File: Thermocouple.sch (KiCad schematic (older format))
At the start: 31 parts, among them P2 CONN_3X2, P3 CONN_2, U2 MCP3901, U3 LMT84, U4 OPA4170

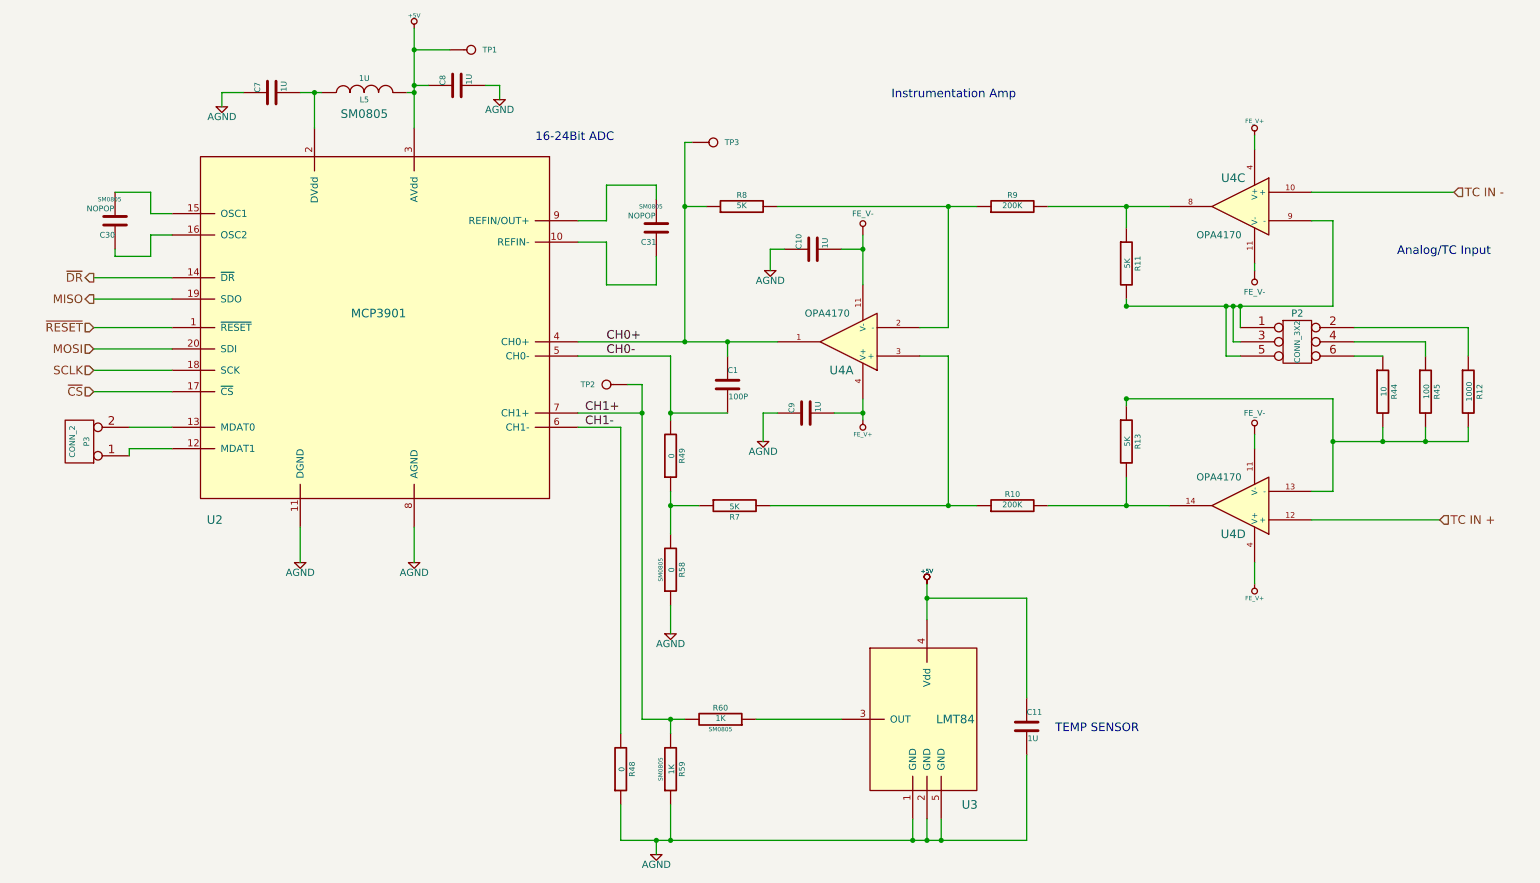
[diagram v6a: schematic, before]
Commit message: Added the schematic and BOM changes back in after hard reset
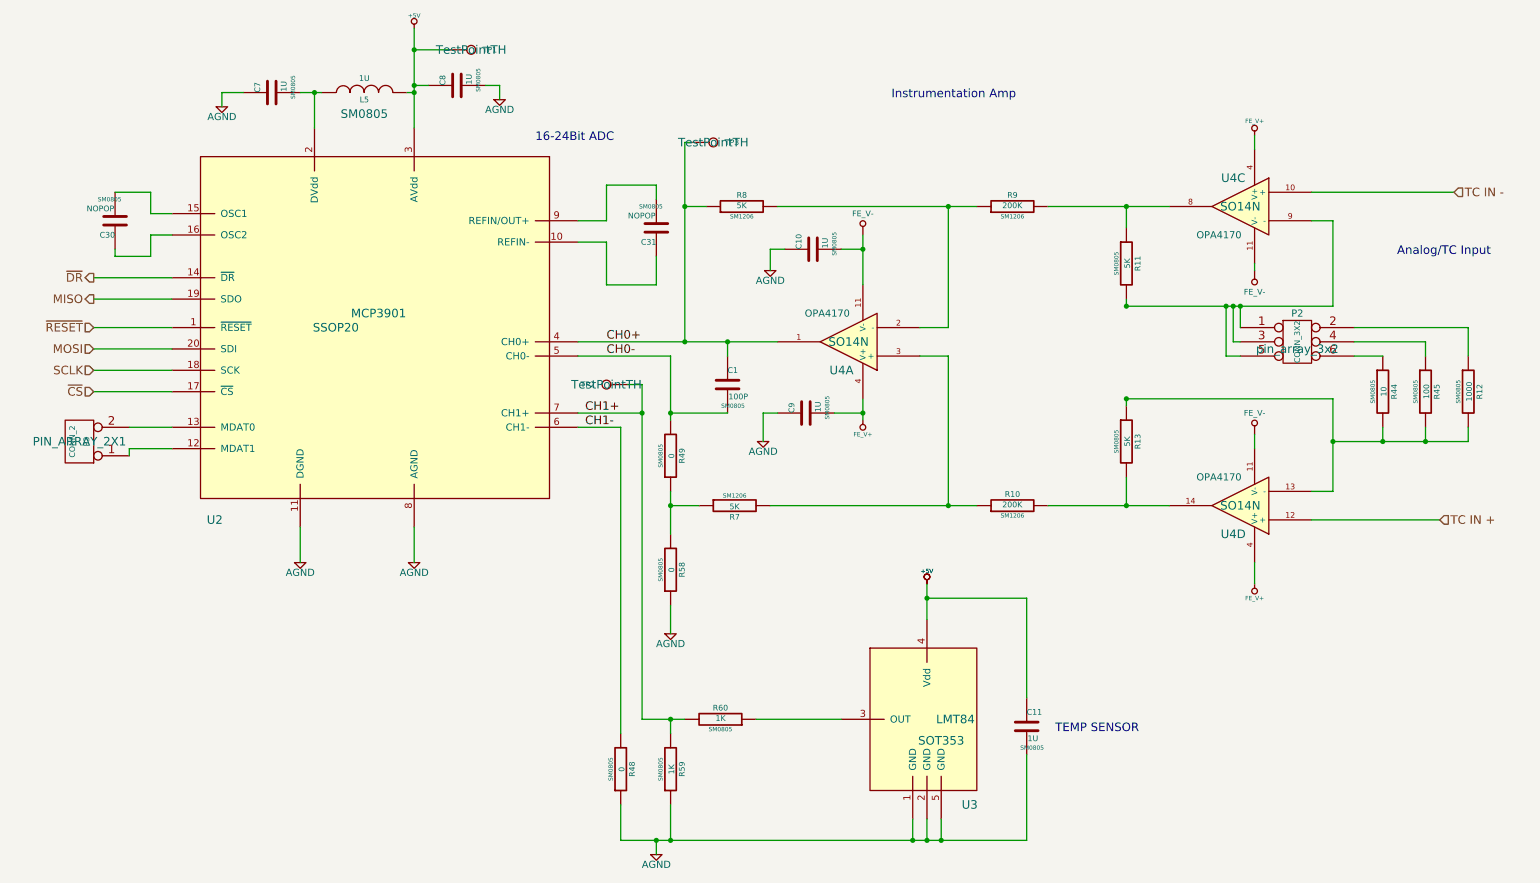
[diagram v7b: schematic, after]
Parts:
- C1, C10, C11, C7, C8, C9, R11, R12, R13, R44, R45, R48, R49: footprint ~ -> SM0805
- P2: footprint (none) -> pin_array_3x2
- P3: footprint (none) -> PIN_ARRAY_2X1
- R10, R7, R8, R9: footprint ~ -> SM1206
- TP1, TP2, TP3: footprint (none) -> TestPointTH
- U2: footprint (none) -> SSOP20
- U3: footprint (none) -> SOT353
- U4: footprint (none) -> SO14N
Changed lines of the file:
@@
-EESchema Schematic File Version 2  date 4/16/2014 11:04:06 PM
+EESchema Schematic File Version 2  date 4/18/2014 9:49:53 PM
 LIBS:power
 LIBS:device
@@
 Sheet 2 9
 Title ""
-Date "17 apr 2014"
+Date "19 apr 2014"
 Rev ""
 Comp ""
@@
 F 0 "U4" H 8950 2550 60  0000 C CNN
 F 1 "OPA4170" H 9050 2150 50  0000 C CNN
-F 2 "" H 8900 2350 60  0000 C CNN
+F 2 "SO14N" H 8900 2350 60  0000 C CNN
 F 3 "" H 8900 2350 60  0000 C CNN
 	3    8900 2350
@@
 F 0 "U4" H 8950 4650 60  0000 C CNN
 F 1 "OPA4170" H 9050 4250 50  0000 C CNN
-F 2 "" H 8900 4450 60  0000 C CNN
+F 2 "SO14N" H 8900 4450 60  0000 C CNN
 F 3 "" H 8900 4450 60  0000 C CNN
 	4    8900 4450
@@
 F 0 "U4" H 6200 3500 60  0000 C CNN
 F 1 "OPA4170" H 6300 3100 50  0000 C CNN
-F 2 "" H 6150 3300 60  0000 C CNN
+F 2 "SO14N" H 6150 3300 60  0000 C CNN
 F 3 "" H 6150 3300 60  0000 C CNN
 	1    6150 3300
@@
 F 0 "C1" H 5300 3700 40  0000 L CNN
 F 1 "100P" H 5306 3515 40  0000 L CNN
-F 2 "~" H 5338 3450 30  0000 C CNN
+F 2 "SM0805" H 5338 3450 30  0000 C CNN
 F 3 "~" H 5300 3600 60  0000 C CNN
 	1    5300 3600
@@
 F 0 "R11" V 8180 2750 40  0000 C CNN
 F 1 "5K" V 8107 2751 40  0000 C CNN
-F 2 "~" V 8030 2750 30  0000 C CNN
+F 2 "SM0805" V 8030 2750 30  0000 C CNN
 F 3 "~" H 8100 2750 30  0000 C CNN
 	1    8100 2750
@@
 F 0 "R12" V 10580 3650 40  0000 C CNN
 F 1 "1000" V 10507 3651 40  0000 C CNN
-F 2 "~" V 10430 3650 30  0000 C CNN
+F 2 "SM0805" V 10430 3650 30  0000 C CNN
 F 3 "~" H 10500 3650 30  0000 C CNN
 	1    10500 3650
@@
 F 0 "R13" V 8180 4000 40  0000 C CNN
 F 1 "5K" V 8107 4001 40  0000 C CNN
-F 2 "~" V 8030 4000 30  0000 C CNN
+F 2 "SM0805" V 8030 4000 30  0000 C CNN
 F 3 "~" H 8100 4000 30  0000 C CNN
 	1    8100 4000
@@
 F 0 "R9" V 7380 2350 40  0000 C CNN
 F 1 "200K" V 7307 2351 40  0000 C CNN
-F 2 "~" V 7230 2350 30  0000 C CNN
+F 2 "SM1206" V 7230 2350 30  0000 C CNN
 F 3 "~" H 7300 2350 30  0000 C CNN
 	1    7300 2350
@@
 F 0 "R8" V 5480 2350 40  0000 C CNN
 F 1 "5K" V 5407 2351 40  0000 C CNN
-F 2 "~" V 5330 2350 30  0000 C CNN
+F 2 "SM1206" V 5330 2350 30  0000 C CNN
 F 3 "~" H 5400 2350 30  0000 C CNN
 	1    5400 2350
@@
 F 0 "R7" V 5430 4450 40  0000 C CNN
 F 1 "5K" V 5357 4451 40  0000 C CNN
-F 2 "~" V 5280 4450 30  0000 C CNN
+F 2 "SM1206" V 5280 4450 30  0000 C CNN
 F 3 "~" H 5350 4450 30  0000 C CNN
 	1    5350 4450
@@
 F 0 "R10" V 7380 4450 40  0000 C CNN
 F 1 "200K" V 7307 4451 40  0000 C CNN
-F 2 "~" V 7230 4450 30  0000 C CNN
+F 2 "SM1206" V 7230 4450 30  0000 C CNN
 F 3 "~" H 7300 4450 30  0000 C CNN
 	1    7300 4450
@@
 F 0 "U2" H 4000 2050 60  0000 C CNN
 F 1 "MCP3901" H 2850 3500 60  0000 C CNN
-F 2 "" H 3150 3400 60  0000 C CNN
+F 2 "SSOP20" H 3150 3400 60  0000 C CNN
 F 3 "" H 3150 3400 60  0000 C CNN
 	1    2850 3300
@@
 F 0 "R44" V 9980 3650 40  0000 C CNN
 F 1 "10" V 9907 3651 40  0000 C CNN
-F 2 "~" V 9830 3650 30  0000 C CNN
+F 2 "SM0805" V 9830 3650 30  0000 C CNN
 F 3 "~" H 9900 3650 30  0000 C CNN
 	1    9900 3650
@@
 F 0 "R45" V 10280 3650 40  0000 C CNN
 F 1 "100" V 10207 3651 40  0000 C CNN
-F 2 "~" V 10130 3650 30  0000 C CNN
+F 2 "SM0805" V 10130 3650 30  0000 C CNN
 F 3 "~" H 10200 3650 30  0000 C CNN
 	1    10200 3650
@@
 F 0 "P2" H 9300 3600 50  0000 C CNN
 F 1 "CONN_3X2" V 9300 3400 40  0000 C CNN
-F 2 "" H 9300 3350 60  0000 C CNN
+F 2 "pin_array_3x2" H 9300 3350 60  0000 C CNN
 F 3 "" H 9300 3350 60  0000 C CNN
 	1    9300 3350
@@
 F 0 "U3" H 7000 5650 60  0000 C CNN
 F 1 "LMT84" H 6900 6250 60  0000 C CNN
-F 2 "" H 6800 6100 60  0000 C CNN
+F 2 "SOT353" H 6800 6100 60  0000 C CNN
 F 3 "" H 6800 6100 60  0000 C CNN
 	1    6700 6100
@@
 F 0 "C11" H 7400 6100 40  0000 L CNN
 F 1 "1U" H 7406 5915 40  0000 L CNN
-F 2 "~" H 7438 5850 30  0000 C CNN
+F 2 "SM0805" H 7438 5850 30  0000 C CNN
 F 3 "~" H 7400 6000 60  0000 C CNN
 	1    7400 6000
@@
 F 0 "C9" H 5850 3900 40  0000 L CNN
 F 1 "1U" H 5856 3715 40  0000 L CNN
-F 2 "~" H 5888 3650 30  0000 C CNN
+F 2 "SM0805" H 5888 3650 30  0000 C CNN
 F 3 "~" H 5850 3800 60  0000 C CNN
 	1    5850 3800
@@
 F 0 "C10" H 5900 2750 40  0000 L CNN
 F 1 "1U" H 5906 2565 40  0000 L CNN
-F 2 "~" H 5938 2500 30  0000 C CNN
+F 2 "SM0805" H 5938 2500 30  0000 C CNN
 F 3 "~" H 5900 2650 60  0000 C CNN
 	1    5900 2650
@@
 F 0 "C8" H 3400 1600 40  0000 L CNN
 F 1 "1U" H 3406 1415 40  0000 L CNN
-F 2 "~" H 3438 1350 30  0000 C CNN
+F 2 "SM0805" H 3438 1350 30  0000 C CNN
 F 3 "~" H 3400 1500 60  0000 C CNN
 	1    3400 1500
@@
 F 0 "C7" H 2100 1650 40  0000 L CNN
 F 1 "1U" H 2106 1465 40  0000 L CNN
-F 2 "~" H 2138 1400 30  0000 C CNN
+F 2 "SM0805" H 2138 1400 30  0000 C CNN
 F 3 "~" H 2100 1550 60  0000 C CNN
 	1    2100 1550
@@
 F 0 "P3" V 700 4000 40  0000 C CNN
 F 1 "CONN_2" V 800 4000 40  0000 C CNN
-F 2 "" H 750 4000 60  0000 C CNN
+F 2 "PIN_ARRAY_2X1" H 750 4000 60  0000 C CNN
 F 3 "" H 750 4000 60  0000 C CNN
 	1    750  4000
@@
 F 0 "R49" V 4980 4100 40  0000 C CNN
 F 1 "0" V 4907 4101 40  0000 C CNN
-F 2 "~" V 4830 4100 30  0000 C CNN
+F 2 "SM0805" V 4830 4100 30  0000 C CNN
 F 3 "~" H 4900 4100 30  0000 C CNN
 	1    4900 4100
@@
 F 0 "R48" V 4630 6300 40  0000 C CNN
 F 1 "0" V 4557 6301 40  0000 C CNN
-F 2 "~" V 4480 6300 30  0000 C CNN
+F 2 "SM0805" V 4480 6300 30  0000 C CNN
 F 3 "~" H 4550 6300 30  0000 C CNN
 	1    4550 6300
@@
 F 0 "TP3" H 5280 1900 40  0000 L CNN
 F 1 "CH0" H 5200 1955 30  0001 C CNN
-F 2 "" H 5200 1900 60  0000 C CNN
+F 2 "TestPointTH" H 5200 1900 60  0000 C CNN
 F 3 "" H 5200 1900 60  0000 C CNN
 	1    5200 1900
@@
 F 0 "TP2" H 4530 3600 40  0000 L CNN
 F 1 "CH1" H 4450 3655 30  0001 C CNN
-F 2 "" H 4450 3600 60  0000 C CNN
+F 2 "TestPointTH" H 4450 3600 60  0000 C CNN
 F 3 "" H 4450 3600 60  0000 C CNN
 	1    4450 3600
@@
 F 0 "TP1" H 3580 1250 40  0000 L CNN
 F 1 "5V" H 3500 1305 30  0001 C CNN
-F 2 "" H 3500 1250 60  0000 C CNN
+F 2 "TestPointTH" H 3500 1250 60  0000 C CNN
 F 3 "" H 3500 1250 60  0000 C CNN
 	1    3500 1250
